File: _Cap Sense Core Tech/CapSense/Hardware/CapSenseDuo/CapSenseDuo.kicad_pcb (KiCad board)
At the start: 2 copper layers, 22 parts, among them IC1 FDC2214QRGHRQ1, J1 Conn_01x07, J2 Conn_01x08, Y1 ECS-2033-400-BN

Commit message: layout pre route
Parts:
- added A1: Adafruit_Feather_Generic, Module:Adafruit_Feather, B.Cu at (121.8, 106.4)
- added C10: C, Capacitor_SMD:C_0603_1608Metric, F.Cu at (106.5, 123.6)
- added C11: C, Capacitor_SMD:C_0603_1608Metric, F.Cu at (104.6, 123.6)
- added C12: Device_C, Capacitor_SMD:C_0603_1608Metric, F.Cu at (119.1, 115.1)
- added C13: Device_C, Capacitor_SMD:C_0603_1608Metric, F.Cu at (119.1, 119.0)
- added C14: Device_C, Capacitor_SMD:C_0603_1608Metric, F.Cu at (119.1, 123.4)
- added C15: Device_C, Capacitor_SMD:C_0603_1608Metric, F.Cu at (119.2, 127.3)
- added C9: C, Capacitor_SMD:C_0603_1608Metric, F.Cu at (108.4, 123.6)
- added IC2: FDC2214QRGHRQ1, FDC2214:FDC2214RGHR, F.Cu at (111.8, 120.8)
- added L5: L0806C470MPWST, SamacSys:INDC2018X180N, F.Cu at (116.6, 115.1)
- added L6: L0806C470MPWST, SamacSys:INDC2018X180N, F.Cu at (116.6, 119.0)
- added L7: L0806C470MPWST, SamacSys:INDC2018X180N, F.Cu at (116.6, 123.2)
- added L8: L0806C470MPWST, SamacSys:INDC2018X180N, F.Cu at (116.7, 127.2)
- added R1: R, Resistor_SMD:R_0603_1608Metric_Pad0.98x0.95mm_HandSolder, F.Cu at (113.7, 129.3)
- added R2: R, Resistor_SMD:R_0603_1608Metric_Pad0.98x0.95mm_HandSolder, F.Cu at (111.4, 126.6)
- added R9: R, Resistor_SMD:R_0603_1608Metric_Pad0.98x0.95mm_HandSolder, F.Cu at (104.9, 129.7)
- added SW1: SW_Push_DPDT, SamacSys:2mm-DPDT, B.Cu at (125.2, 106.4)
- C1, C4: value 0.01uF -> C
- C2: value 1uF -> C
- C3: value 0.1uF -> C
- C5, C6, C7, C8: value 33pF -> C
- IC1: value FDC2214QRGHRQ1 -> FDC2214-rescue_FDC2214QRGHRQ1-SamacSys_Parts; footprint QFN50P400X400X80-17N -> FDC2214:FDC2214RGHR
- J1: value Conn_01x07 -> Conn_01x08; footprint Connector_PinHeader_2.54mm:PinHeader_1x07_P2.54mm_Vertical -> Connector_PinHeader_2.54mm:PinHeader_1x08_P2.54mm_Vertical
- L1, L2, L3, L4: value CMH322522-180KL -> L0806C470MPWST; footprint INDPM3225X240N -> SamacSys:INDC2018X180N
- R3: value 0 -> R
- R4, R5, R6: value 49 -> R
- moved R6 78.6 mm to (105.3, 135.5)
- moved R5 78.6 mm to (105.3, 137.3)
- moved R4 78.2 mm to (104.8, 131.2), turned to 0 degrees
- moved R3 75.6 mm to (104.8, 132.8)
- moved R8 74.0 mm to (107.9, 118.2)
- moved R7 73.9 mm to (107.9, 116.6)
- moved C1 72.2 mm to (109.0, 129.3)
- moved IC1 71.8 mm to (111.8, 137.6)
- moved C8 71.7 mm to (119.1, 143.8)
- moved L4 71.7 mm to (116.8, 143.6)
- moved C7 71.7 mm to (119.1, 139.4)
- moved L3 71.7 mm to (116.8, 139.4)
- moved C2 71.7 mm to (109.6, 140.9)
- moved C3 71.7 mm to (108.1, 140.9)
- moved C4 71.7 mm to (106.5, 140.9)
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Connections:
- IC1 pad 3: Net-(IC1-Pad3) -> clk
- IC1 pad 4: ADDR -> ADDR1
- IC1 pad 5: INTB -> INTB1
- J1 pad 1: GND -> IN0A
- J1 pad 2: SD -> IN0B
- J1 pad 3: INTB -> IN1A
- J1 pad 4: ADDR -> IN1B
- J1 pad 5: +3V3 -> IN2A
- J1 pad 6: SDA -> IN2B
- J1 pad 7: SCL -> IN3A
- J2 pad 1: IN3B -> IN4A
- J2 pad 2: IN3A -> IN4B
- J2 pad 3: IN2B -> IN5A
- J2 pad 4: IN2A -> IN5B
- J2 pad 5: IN1B -> IN6A
- J2 pad 6: IN1A -> IN6B
- J2 pad 7: IN0B -> IN7A
- J2 pad 8: IN0A -> IN7B
- R3 pad 1: Net-(R3-Pad1) -> +3V3
- R3 pad 2: Net-(IC1-Pad3) -> SDA
- R4 pad 1: Net-(IC1-Pad3) -> +3V3
- R4 pad 2: GND -> SCL
- R5 pad 2: SDA -> ADDR1
- R6 pad 1: +3V3 -> ADDR1
- R6 pad 2: SCL -> GND
- R7 pad 2: ADDR -> ADDR2
- R8 pad 1: ADDR -> ADDR2
- Y1 pad 1: Net-(Y1-Pad1) -> unconnected-(Y1-Pad1)
- Y1 pad 3: Net-(R3-Pad1) -> Net-(R1-Pad1)
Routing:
- net (no net): vias 0 -> 4
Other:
- board outline added: 30.8 x 51.3 mm
- net class Default removed
- board text added: "BAT"
- board text added: "USB"

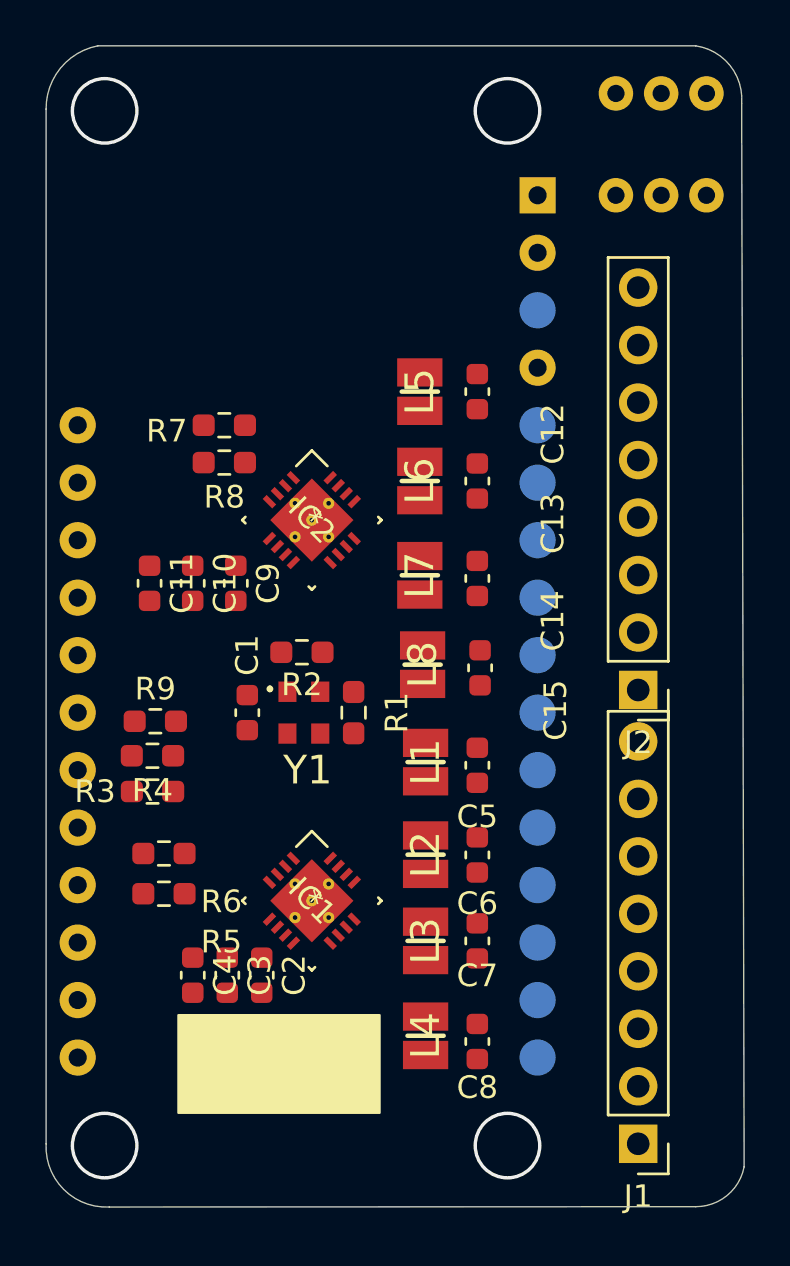
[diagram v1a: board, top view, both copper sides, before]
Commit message: place and route finished for CapDuo
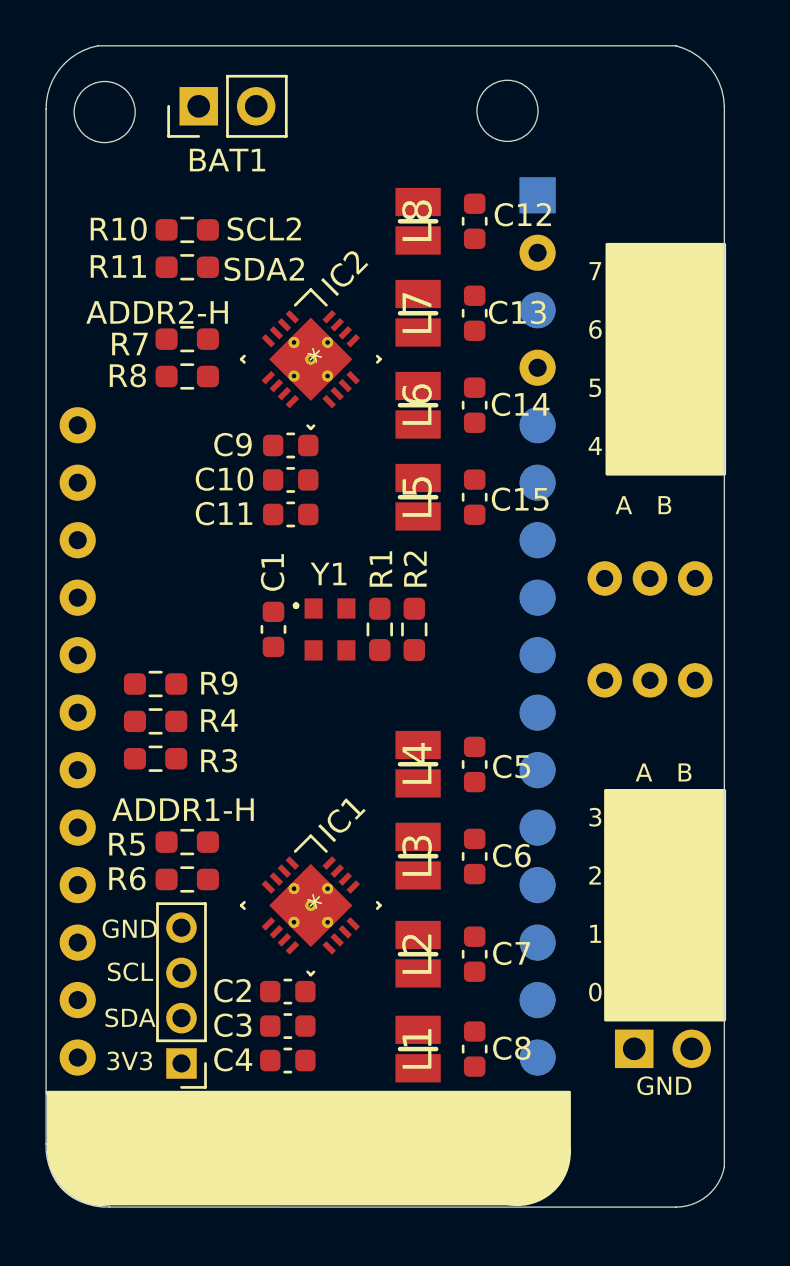
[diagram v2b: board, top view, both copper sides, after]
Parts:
- added BAT1: Conn_01x02, Connector_PinHeader_2.54mm:PinHeader_1x02_P2.54mm_Vertical, F.Cu at (106.8, 102.5)
- added H1: MountingHole, MountingHole:MountingHole_2.7mm_M2.5, F.Cu at (102.7, 102.7)
- added H2: MountingHole, MountingHole:MountingHole_2.7mm_M2.5, F.Cu at (120.5, 102.7)
- added H3: MountingHole, MountingHole:MountingHole_2.7mm_M2.5, F.Cu at (102.7, 148.4)
- added H4: MountingHole, MountingHole:MountingHole_2.7mm_M2.5, F.Cu at (120.5, 148.4)
- added J3: Conn_02x01, Connector_PinHeader_2.54mm:PinHeader_2x01_P2.54mm_Horizontal, B.Cu at (126.0, 144.1)
- added R10: R, Resistor_SMD:R_0603_1608Metric_Pad0.98x0.95mm_HandSolder, F.Cu at (106.3, 108.0)
- added R11: R, Resistor_SMD:R_0603_1608Metric_Pad0.98x0.95mm_HandSolder, F.Cu at (106.3, 109.6)
- added test1: Conn_01x04, Connector_PinHeader_2.00mm:PinHeader_1x04_P2.00mm_Vertical, F.Cu at (106.0, 144.8)
- J1, J2: value Conn_01x08 -> Conn_02x04_Odd_Even; footprint Connector_PinHeader_2.54mm:PinHeader_1x08_P2.54mm_Vertical -> Connector_PinHeader_2.54mm:PinHeader_2x04_P2.54mm_Horizontal; moved to B.Cu
- moved SW1 21.4 mm to (124.7, 127.9)
- moved J2 10.8 mm to (126.0, 117.5), turned to 0 degrees
- moved C14 7.65 mm to (119.0, 115.7)
- moved C15 7.54 mm to (119.0, 119.8)
- moved C12 7.53 mm to (119.0, 107.6)
- moved L8 7.53 mm to (116.5, 107.6)
- moved L6 7.51 mm to (116.5, 115.7)
- moved C13 7.41 mm to (119.0, 111.6)
- moved L7 7.41 mm to (116.5, 111.6)
- moved L5 7.40 mm to (116.5, 119.8)
- moved IC2 7.11 mm to (111.8, 113.7)
- moved C11 6.94 mm to (110.9, 120.5), turned to 0 degrees
- moved J1 6.74 mm to (126.0, 141.6), turned to 0 degrees
- moved C9 6.56 mm to (110.9, 117.5), turned to 0 degrees
- moved C10 6.29 mm to (110.9, 119.0), turned to 0 degrees
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- renumbered L4 to L1, L3 to L2, L2 to L3, L1 to L4, L8 to L5, L7 to L6, L6 to L7, L5 to L8
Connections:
- A1 pad 28: unconnected-(A1-Pad28) -> VBAT
- IC2 pad 1: SCL -> SCL2
- IC2 pad 2: SDA -> SDA2
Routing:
- net (no net): vias 4 -> 0
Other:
- board size 30.8 x 51.3 mm -> 30 x 51.3 mm
- board text added: "3 2 1 0"
- board text added: "3V3"
- board text added: "7 6 5 4"
- board text added: "A B"
- board text added: "ADDR1-H"
- board text added: "ADDR2-H"
- board text added: "GND"
- board text added: "SCL"
- board text added: "SCL2"
- board text added: "SDA"
- board text added: "SDA2"

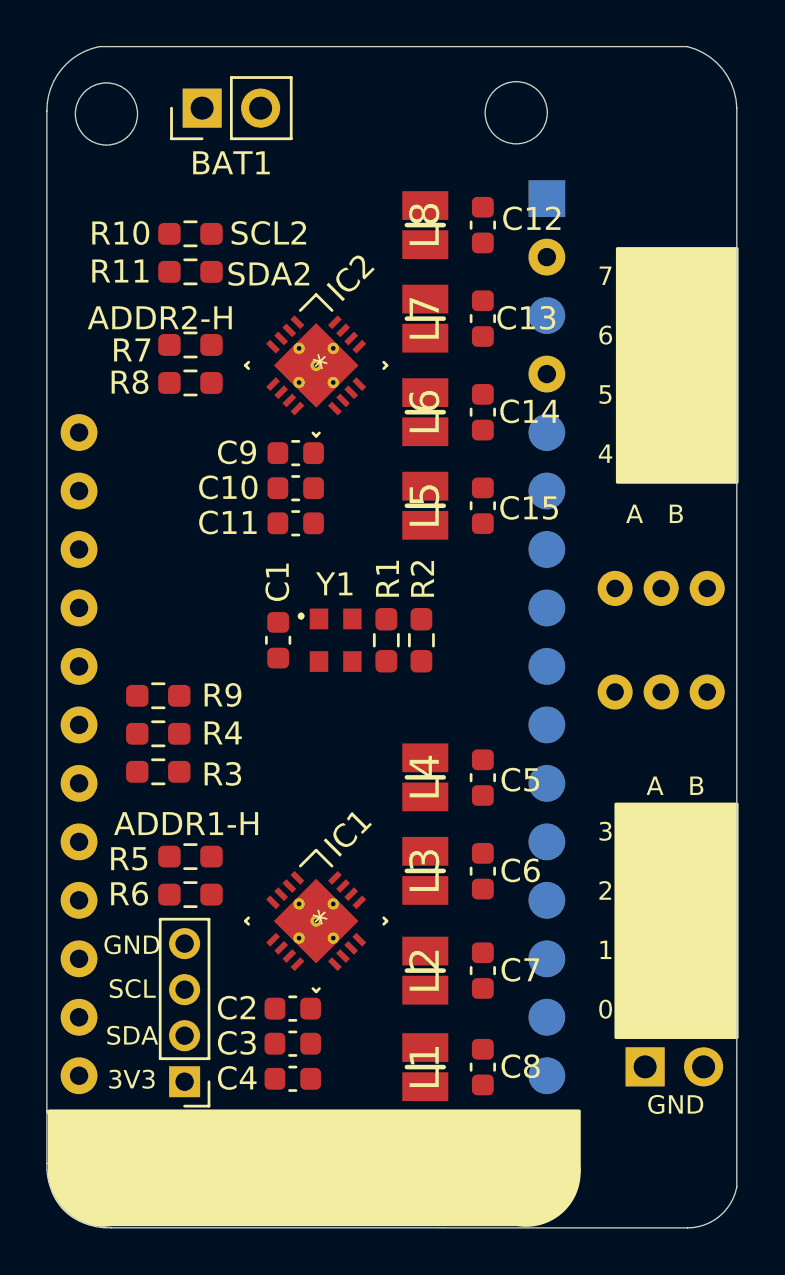
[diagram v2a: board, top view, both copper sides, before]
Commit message: created Quadro project for future 4x FDC
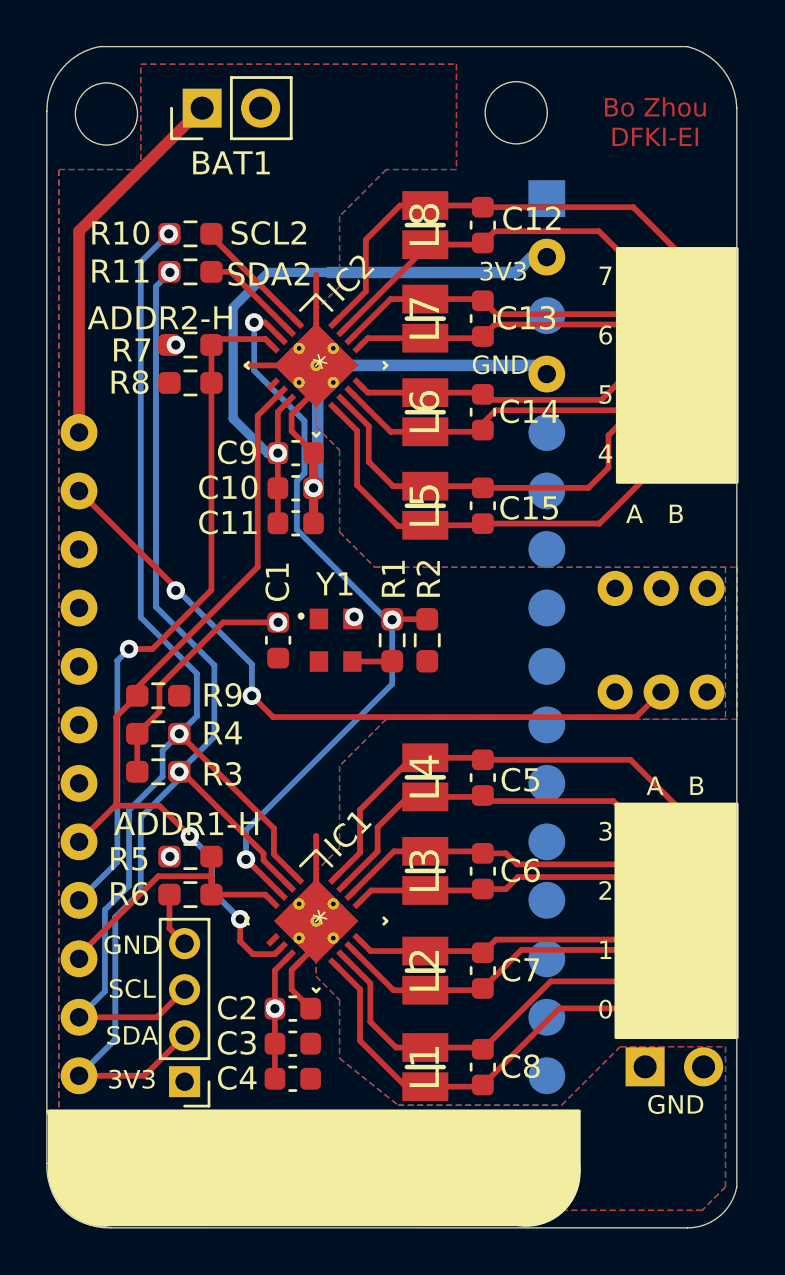
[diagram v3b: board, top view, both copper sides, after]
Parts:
- moved R2 0.25 mm to (116.6, 125.6)
- moved R1 0.25 mm to (115.1, 125.6)
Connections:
- C10 pad 1: Net-(C10-Pad1) -> +3V3
- C11 pad 1: Net-(C10-Pad1) -> +3V3
- C2 pad 1: Net-(C2-Pad1) -> +3V3
- C3 pad 1: Net-(C2-Pad1) -> +3V3
- C4 pad 1: Net-(C2-Pad1) -> +3V3
- C9 pad 1: Net-(C10-Pad1) -> +3V3
- IC1 pad 7: Net-(C2-Pad1) -> +3V3
- IC1 pad V: (no net) -> GND
- IC2 pad 7: Net-(C10-Pad1) -> +3V3
- IC2 pad V: (no net) -> GND
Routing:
- net SCL: track 0.00 -> 51.1 mm, vias 0 -> 2
- net SDA: track 0.00 -> 50.9 mm, vias 0 -> 2
- net +3V3: track 0.00 -> 43.5 mm, vias 0 -> 6
- net GND: track 0.00 -> 37.4 mm, vias 0 -> 1
- net SD: track 0.00 -> 34.6 mm, vias 0 -> 2
- net clk: track 0.00 -> 33.7 mm, vias 0 -> 3
- net Net-(A1-Pad27): track 0.00 -> 30.7 mm, vias 0 -> 2
- net ADDR2: track 0.00 -> 30.0 mm, vias 0 -> 1
- net IN7B: track 0.00 -> 20.7 mm
- net IN3B: track 0.00 -> 20.6 mm
- net IN4B: track 0.00 -> 20.6 mm
- net IN0B: track 0.00 -> 20.0 mm
- net IN4A: track 0.00 -> 18.9 mm
- net IN0A: track 0.00 -> 18.4 mm
- net IN6B: track 0.00 -> 16.9 mm
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- added copper zone on B.Cu, net +3V3
- added copper zone on F.Cu, net GND
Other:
- board text added: "Bo Zhou DFKI-EI"
